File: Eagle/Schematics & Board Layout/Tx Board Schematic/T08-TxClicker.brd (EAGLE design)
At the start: 88.9 x 44.5 mm, 78 parts, among them Q1 DMN63D8LDW, Q2 DMN63D8LDW, U1 CC430F513X---RGZ48, Y1 9C-26.000MEEJ-T

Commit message: Layout Work
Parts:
- C23, C24, C25, C26, C27, C28, C29, C35, C6, C7, C8, C9: device rcl:C0603 -> rcl-amber:C0603
- moved L7 121.6 mm to (61.5, 32.8), turned to 90 degrees
- moved L6 119.9 mm to (61.7, 30.5), turned to 270 degrees
- moved C25 118.6 mm to (54.9, 34.3), turned to 270 degrees
- moved L5 115.4 mm to (59.9, 32.0)
- moved C24 114.3 mm to (56.4, 28.7)
- moved C23 109.8 mm to (54.1, 31.8), turned to 270 degrees
- moved L4 108.7 mm to (54.9, 29.5), turned to 270 degrees
- moved L3 106.1 mm to (55.6, 32.8), turned to 180 degrees
- moved L2 100.8 mm to (52.6, 32.5), turned to 180 degrees
- moved C29 99.9 mm to (62.2, 34.3), turned to 180 degrees
- moved L1 98.8 mm to (52.6, 31.0), turned to 180 degrees
- moved C28 92.7 mm to (60.7, 30.5), turned to 90 degrees
- moved C27 83.1 mm to (57.7, 32.0)
- moved C26 75.1 mm to (55.6, 31.0), turned to 180 degrees
- moved C9 72.8 mm to (40.1, 42.2), turned to 90 degrees
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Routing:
- net PJ.3/TCK: track 0.00 -> 11.5 mm
- net PJ.2/TMS: track 0.00 -> 11.2 mm
- net PJ.1/TDI/TCLK: track 0.00 -> 10.7 mm
- net PJ.0/TDO: track 0.00 -> 9.73 mm
- net GND: track 0.00 -> 4.12 mm, vias 0 -> 54
- net N$10: track 0.00 -> 3.90 mm
- net N$6: track 0.00 -> 3.04 mm
- net N$3: track 0.00 -> 2.98 mm
- net N$2: track 0.00 -> 2.91 mm
- net N$1: track 0.00 -> 2.60 mm
- net N$7: track 0.00 -> 1.79 mm
- net RF_P: track 0.00 -> 1.75 mm
- net RF_N: track 0.00 -> 1.75 mm
- net RST/NMI/SBWTDIO: track 0.00 -> 1.59 mm
- net N$5: track 0.00 -> 0.89 mm
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
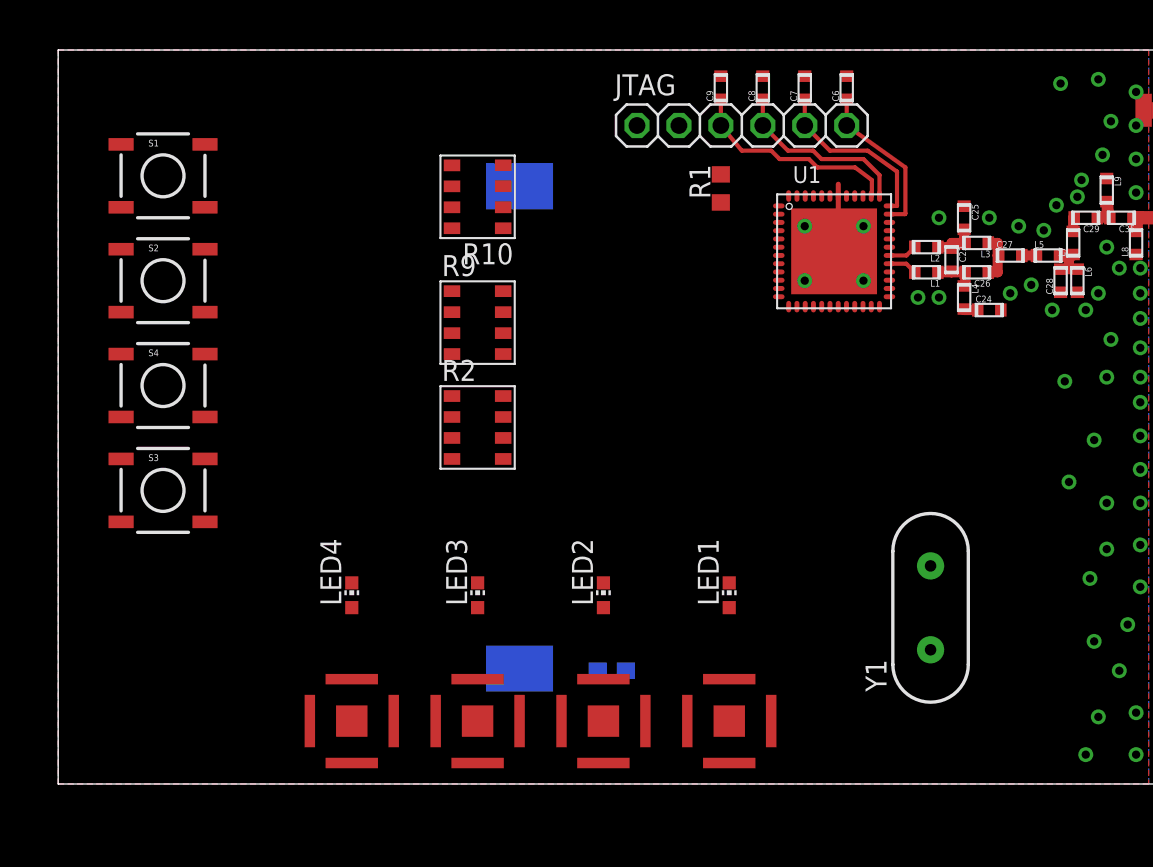
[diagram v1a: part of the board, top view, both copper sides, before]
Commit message: Materials BOM
Created BOM, made pushbuttons larger on PCB
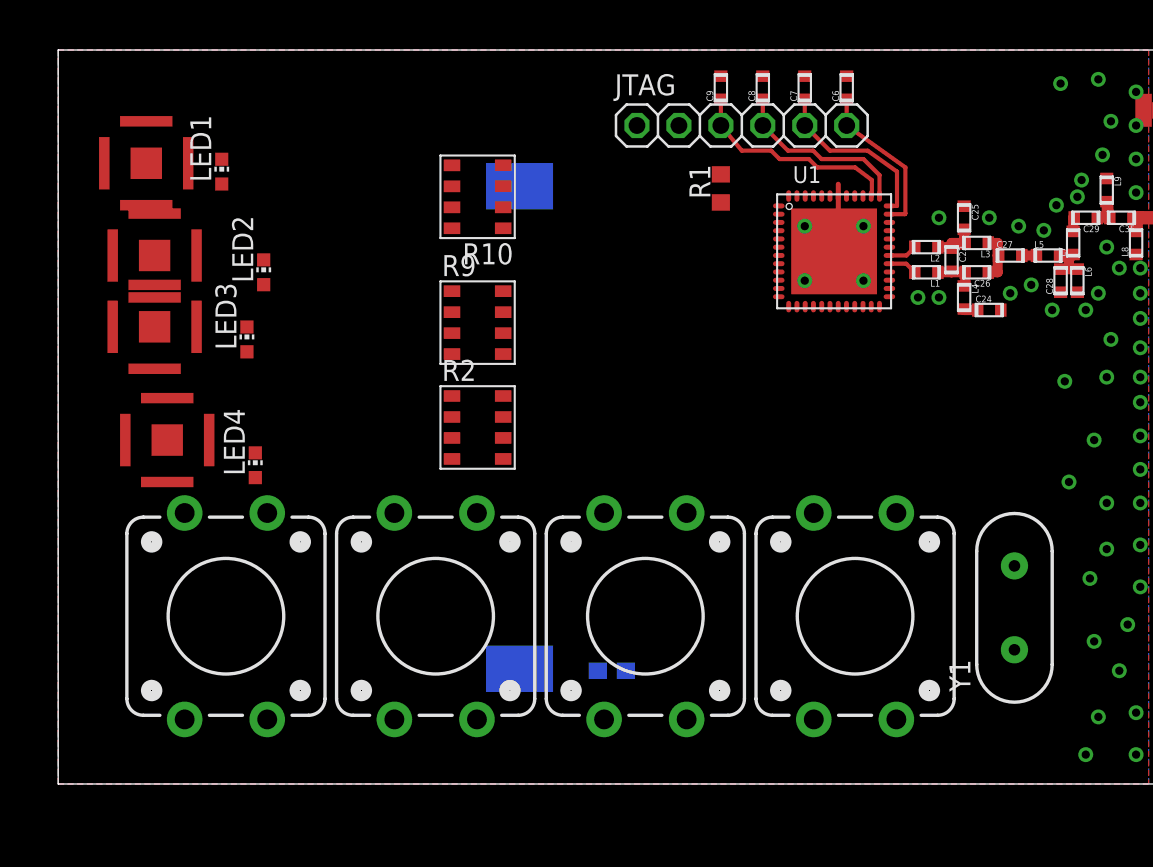
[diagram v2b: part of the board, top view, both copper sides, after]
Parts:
- S1, S2, S3, S4: value SWITCH-MOMENTARY-2SMD -> SWITCH-MOMENTARY-212MM; device SparkFun-Electromechanical:TACTILE_SWITCH_SMD -> SparkFun-Electromechanical:TACTILE-PTH-12MM
- moved S1 49.7 mm to (48.3, 10.2), turned to 90 degrees
- moved U$1 44.8 mm to (5.84, 32.0)
- moved LED1 40.0 mm to (9.91, 37.1)
- moved U$3 36.0 mm to (5.33, 37.6)
- moved S4 32.4 mm to (35.6, 10.2), turned to 90 degrees
- moved U$4 31.4 mm to (6.60, 20.8)
- moved U$5 30.9 mm to (5.84, 27.7)
- moved LED2 28.4 mm to (12.4, 31.0)
- moved S2 26.2 mm to (22.9, 10.2), turned to 90 degrees
- moved LED3 20.9 mm to (11.4, 26.9)
- moved LED4 9.80 mm to (11.9, 19.3)
- moved S3 8.52 mm to (10.2, 10.2), turned to 90 degrees
- moved Y1 5.08 mm to (57.9, 10.7)

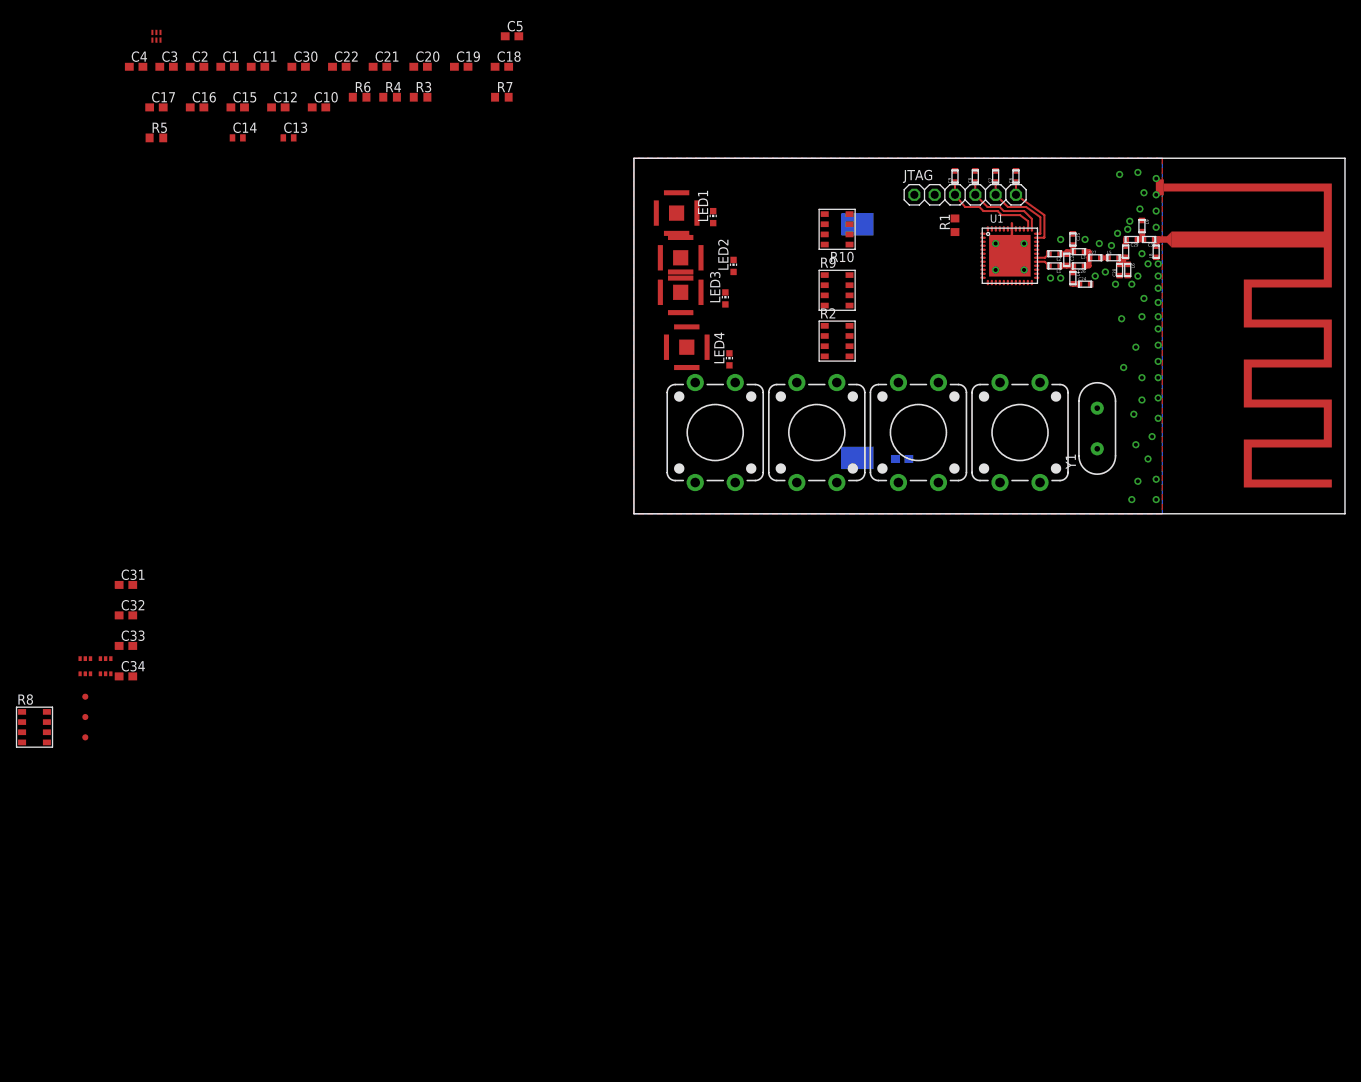
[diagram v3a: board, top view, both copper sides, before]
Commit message: Tx-Schematic Update for Team Review
Removed triple redundant capacitive sensor, removed MOSFET LED drivers,
changed RF signal path to 0402 capacitors from 0603.
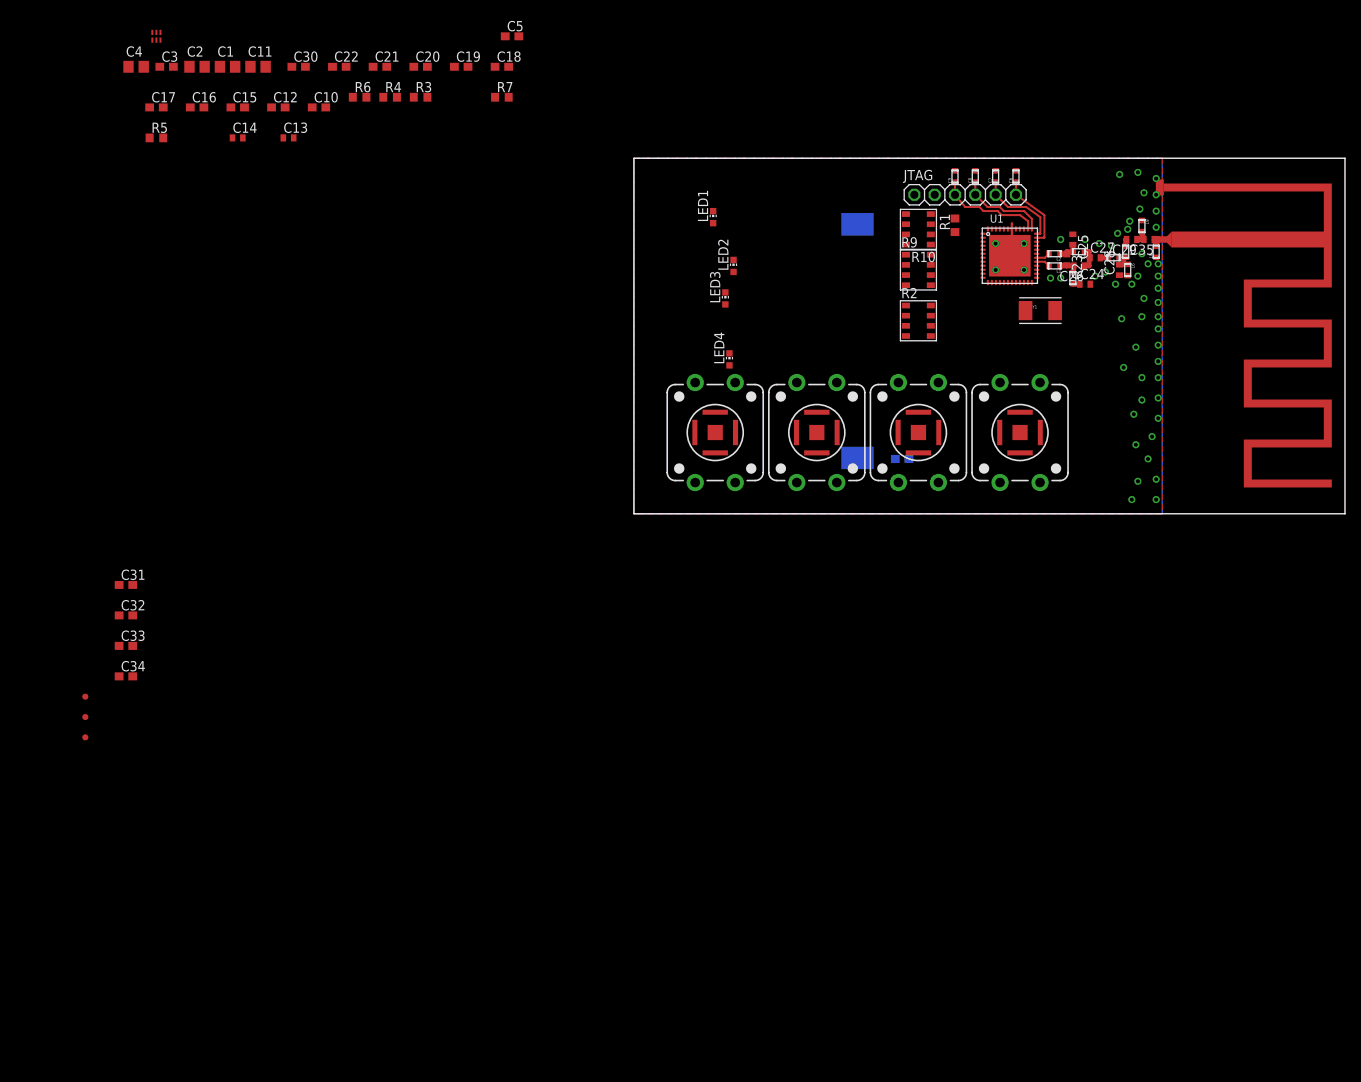
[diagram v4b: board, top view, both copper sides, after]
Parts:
- removed Q1, Q2: DMN63D8LDW, MOSFETS:SOT363
- removed R8: DNI, QuadResistor:2012(4_RES)
- C1, C11, C2, C4: device rcl:C0603 -> rcl:C0805
- C23, C24, C25, C26, C27, C28, C29, C35: device rcl-amber:C0603 -> rcl:C0402
- C6, C7, C8: value 2pF -> 2pF/DNI
- U$2: value CR2032-SNAPDRAGON -> CR2032-SNAPDRAGONCR2032
- Y1: value 9C-26.000MEEJ-T -> (none); device SparkFun-FreqCtrl:HC49US -> SparkFun-FreqCtrl:CRYSTAL-TXC-7A
- moved U$3 50.9 mm to (48.3, 10.2)
- moved U$1 36.9 mm to (35.6, 10.2)
- moved U$5 24.4 mm to (22.9, 10.2)
- moved Y1 16.4 mm to (50.8, 25.4), turned to 0 degrees
- moved U$4 11.2 mm to (10.2, 10.2)
- moved R2 10.5 mm to (35.6, 24.1)
- moved R9 10.5 mm to (35.6, 30.5)
- moved R10 10.2 mm to (35.6, 35.6)
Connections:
- removed net N$14: LED3.C, Q1.3
- removed net N$16: LED4.C, Q1.6
- removed net N$25: LED2.C, Q2.3
- removed net N$26: LED1.C, Q2.6
- removed net P1.0: R8.1, U1.13
- removed net P1.1: R8.3, U1.12
- removed net P1.2: R8.5, U1.11
- removed net P1.3: R8.7, U1.10
- net GND: no longer Q1.1, Q1.4, Q2.1, Q2.4
- net P1.7: no longer R8.8
- net P2.0: no longer R8.6
- net P2.1: no longer R8.4
- net P2.2: no longer R8.2
- net P3.2: now also LED1.C; no longer Q2.2
- net P3.3: now also LED2.C; no longer Q2.5
- net P3.4: now also LED4.C; no longer Q1.2
- net P3.5: now also LED3.C; no longer Q1.5
- net RF_XIN: now also Y1.P$1; no longer Y1.1
- net RF_XOUT: now also Y1.P$2; no longer Y1.2

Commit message: Tx-Schematic update
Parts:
- removed C30: DNI, rcl:C0603
- removed F1: PTC0603, SparkFun-PowerIC:0603
- removed R10: 10k, QuadResistor:2012(4_RES)
- removed R6: 0, rcl:R0603
- removed R7: DNI, rcl:R0603
- added L10: ~200nH, rcl-amber:L0402
- added TP4, TP5, TP6, TP7, TP8: TEST-POINT3, SparkFun-Passives:PAD.03X.03
- JTAG: value (none) -> 6pin
- LED1: value (none) -> Blue
- LED2: value (none) -> Green
- LED3: value (none) -> Red
- LED4: value (none) -> Yellow
- Y1: value (none) -> 26MHz
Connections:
- removed net ADC: R6.1, R7.1, R9.2, R9.4, R9.6, R9.8
- removed net N$13: R10.2, R4.1, S4.1, U$5.P$1, U$5.P$2, U$5.P$3, U$5.P$4
- removed net N$17: R10.3, R10.6, S2.1, U$3.P$1, U$3.P$2, U$3.P$3, U$3.P$4
- removed net N$19: R10.1, R10.4, S3.1, U$4.P$1, U$4.P$2, U$4.P$3, U$4.P$4
- removed net P2.3: C30.1, R7.2, U$6.6, U1.48
- net GND: now also R9.2, R9.4, R9.6, R9.8; no longer C30.2, R6.2
- net N$20: now also R4.1, S2.1, S3.1, S4.1, U$3.P$1, U$3.P$2, U$3.P$3, U$3.P$4, U$4.P$1, U$4.P$2, U$4.P$3, U$4.P$4, U$5.P$1, U$5.P$2, U$5.P$3, U$5.P$4; no longer R10.5
- net N$9: now also C15.1, C16.1, C17.1, C18.1, C19.1, C20.1, C21.1, L10.P$2, U1.27, U1.28, U1.31, U1.32, U1.34; no longer F1.1, U$2.V+
- net P1.7: now also TP7.P$1
- net P2.0: now also TP6.P$1
- net P2.1: now also TP5.P$1
- net P2.2: now also TP4.P$1
- net VCC: now also L10.P$1, TP8.P$1, U$2.V+; no longer C15.1, C16.1, C17.1, C18.1, C19.1, C20.1, C21.1, F1.2, U1.27, U1.28, U1.31, U1.32, U1.34

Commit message: Tx-Schematic Update
Changed pull-down to 10Meg, changed JTAG EMI cap from DNI to 2pF,
Annotated JTAG as Tag-Connect
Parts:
- removed U$6: ESDA6V1-5M6, TVS:5X-TVS
- added D1: ESDA6V1-5M6, TVS:5X-TVS
- C6, C7, C8: value 2pF/DNI -> 2pF
- R9: value 1MEG -> 10MEG
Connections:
- net GND: now also D1.2; no longer U$6.2
- net P1.7: now also D1.5; no longer U$6.1
- net P2.0: now also D1.4; no longer U$6.3
- net P2.1: now also D1.3; no longer U$6.4
- net P2.2: now also D1.1; no longer U$6.5

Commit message: TX_Schematic Update
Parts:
- moved S2 12.7 mm to (10.2, 10.2)
- moved S3 12.7 mm to (22.9, 10.2)
- moved S1 12.7 mm to (35.6, 10.2)
- moved S4 12.7 mm to (48.3, 10.2)
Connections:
- net P1.7: now also S4.3; no longer S1.3
- net P2.0: now also S3.3; no longer S2.3
- net P2.1: now also S2.3; no longer S3.3
- net P2.2: now also S1.3; no longer S4.3
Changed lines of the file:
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@@
 <?xml version="1.0" encoding="utf-8"?>
 <!DOCTYPE eagle SYSTEM "eagle.dtd">
-<eagle version="6.4">
+<eagle version="7.1.0">
 <drawing>
 <settings>
@@
 <pass name="Default">
 <param name="RoutingGrid" value="50mil"/>
+<param name="AutoGrid" value="1"/>
+<param name="Efforts" value="0"/>
+<param name="TopRouterVariant" value="1"/>
 <param name="tpViaShape" value="round"/>
 <param name="PrefDir.1" value="|"/>
@@
 <element name="R2" library="QuadResistor" package="2012(4_RES)" value="3.3k" x="35.56" y="24.13"/>
 <element name="R5" library="rcl" package="R0603" value="DNI" x="-59.69" y="46.99"/>
-<element name="S3" library="SparkFun-Electromechanical" package="TACTILE-PTH-12MM" value="SWITCH-MOMENTARY-212MM" x="10.16" y="10.16" rot="R90">
+<element name="S2" library="SparkFun-Electromechanical" package="TACTILE-PTH-12MM" value="SWITCH-MOMENTARY-212MM" x="10.16" y="10.16" rot="R90">
 <attribute name="PROD_ID" value="SWCH-09185" x="10.16" y="10.16" size="1.778" layer="27" rot="R90" display="off"/>
 </element>
@@
 <element name="L8" library="rcl-amber" package="L0603" value="5.6nH" x="65.278" y="32.766" rot="R90"/>
 <element name="L9" library="rcl-amber" package="L0603" value="DNP" x="63.5" y="35.9664" rot="R270"/>
-<element name="S2" library="SparkFun-Electromechanical" package="TACTILE-PTH-12MM" value="SWITCH-MOMENTARY-212MM" x="22.86" y="10.16" rot="R90">
+<element name="S3" library="SparkFun-Electromechanical" package="TACTILE-PTH-12MM" value="SWITCH-MOMENTARY-212MM" x="22.86" y="10.16" rot="R90">
 <attribute name="PROD_ID" value="SWCH-09185" x="22.86" y="10.16" size="1.778" layer="27" rot="R90" display="off"/>
 </element>
-<element name="S4" library="SparkFun-Electromechanical" package="TACTILE-PTH-12MM" value="SWITCH-MOMENTARY-212MM" x="35.56" y="10.16" rot="R90">
+<element name="S1" library="SparkFun-Electromechanical" package="TACTILE-PTH-12MM" value="SWITCH-MOMENTARY-212MM" x="35.56" y="10.16" rot="R90">
 <attribute name="PROD_ID" value="SWCH-09185" x="35.56" y="10.16" size="1.778" layer="27" rot="R90" display="off"/>
 </element>
-<element name="S1" library="SparkFun-Electromechanical" package="TACTILE-PTH-12MM" value="SWITCH-MOMENTARY-212MM" x="48.26" y="10.16" rot="R90">
+<element name="S4" library="SparkFun-Electromechanical" package="TACTILE-PTH-12MM" value="SWITCH-MOMENTARY-212MM" x="48.26" y="10.16" rot="R90">
 <attribute name="PROD_ID" value="SWCH-09185" x="48.26" y="10.16" size="1.778" layer="27" rot="R90" display="off"/>
 </element>
@@
 <contactref element="U1" pad="3"/>
 <contactref element="C33" pad="1"/>
-<contactref element="S2" pad="3"/>
+<contactref element="S3" pad="3"/>
 <contactref element="R9" pad="3"/>
 <contactref element="TP6" pad="P$1"/>
@@
 <contactref element="U$1" pad="P$3"/>
 <contactref element="R5" pad="1"/>
-<contactref element="S1" pad="1"/>
+<contactref element="S4" pad="1"/>
 <contactref element="U$3" pad="P$4"/>
 <contactref element="U$3" pad="P$2"/>
 <contactref element="U$3" pad="P$1"/>
 <contactref element="U$3" pad="P$3"/>
-<contactref element="S2" pad="1"/>
+<contactref element="S3" pad="1"/>
 <contactref element="U$4" pad="P$4"/>
 <contactref element="U$4" pad="P$3"/>
 <contactref element="U$4" pad="P$1"/>
 <contactref element="U$4" pad="P$2"/>
-<contactref element="S3" pad="1"/>
+<contactref element="S2" pad="1"/>
 <contactref element="U$5" pad="P$1"/>
 <contactref element="U$5" pad="P$2"/>
 <contactref element="R4" pad="1"/>
 <contactref element="U$5" pad="P$4"/>
-<contactref element="S4" pad="1"/>
+<contactref element="S1" pad="1"/>
 <contactref element="U$5" pad="P$3"/>
 <wire x1="48.26" y1="12.7" x2="50.76" y2="16.41" width="0" layer="19" extent="1-1"/>
@@
 <contactref element="R9" pad="7"/>
 <contactref element="C31" pad="1"/>
-<contactref element="S4" pad="3"/>
+<contactref element="S1" pad="3"/>
 <contactref element="U1" pad="1"/>
 <contactref element="TP4" pad="P$1"/>
@@
 <contactref element="U1" pad="4"/>
 <contactref element="C34" pad="1"/>
-<contactref element="S1" pad="3"/>
+<contactref element="S4" pad="3"/>
 <contactref element="R9" pad="1"/>
 <contactref element="TP7" pad="P$1"/>
@@
 <signal name="P2.1">
 <contactref element="U$4" pad="VCC"/>
-<contactref element="S3" pad="3"/>
+<contactref element="S2" pad="3"/>
 <contactref element="R9" pad="5"/>
 <contactref element="U1" pad="2"/>
